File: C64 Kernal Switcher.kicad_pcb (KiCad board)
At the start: 2 copper layers, 20.3 x 47.6 mm, 12 parts, among them J1 Signals, J2 RGB, J3 LED, U1 2364, U2 PIC12F629, U3 27C256

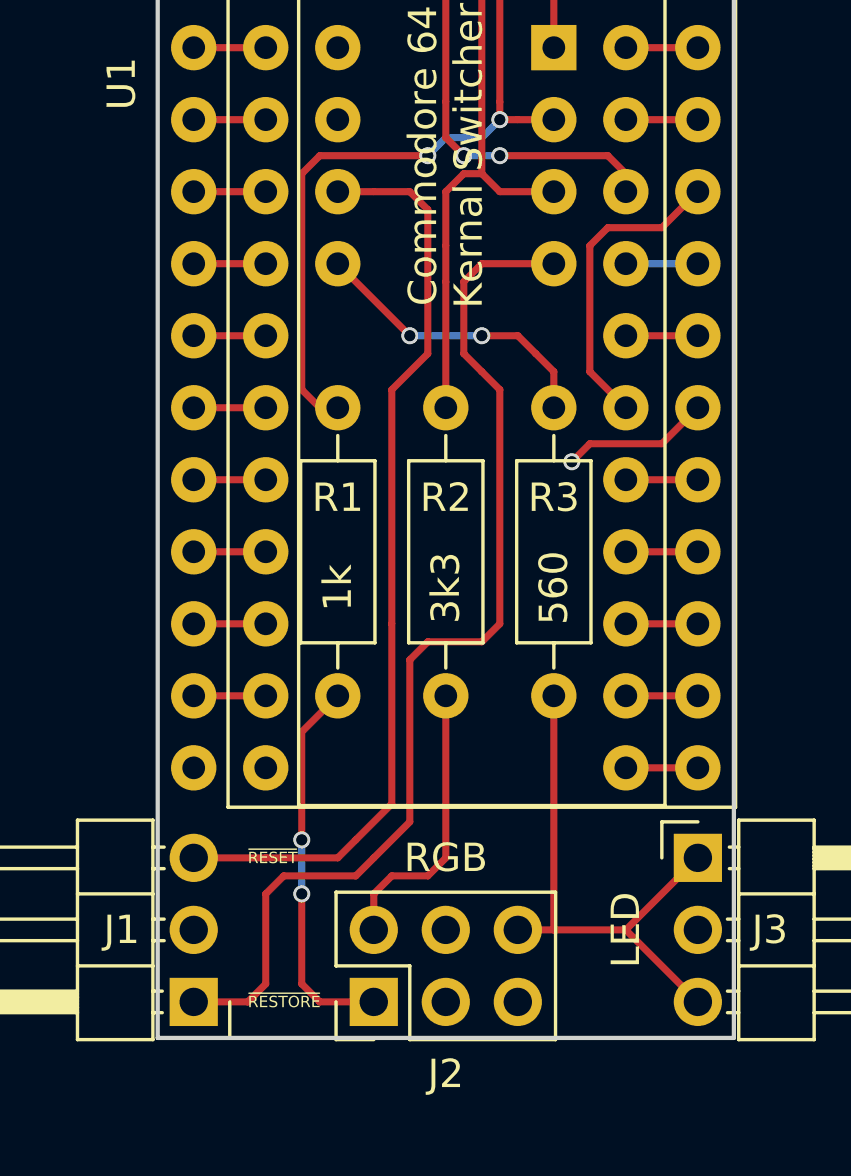
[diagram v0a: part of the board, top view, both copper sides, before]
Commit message: Moved R1 so it fits better under socket
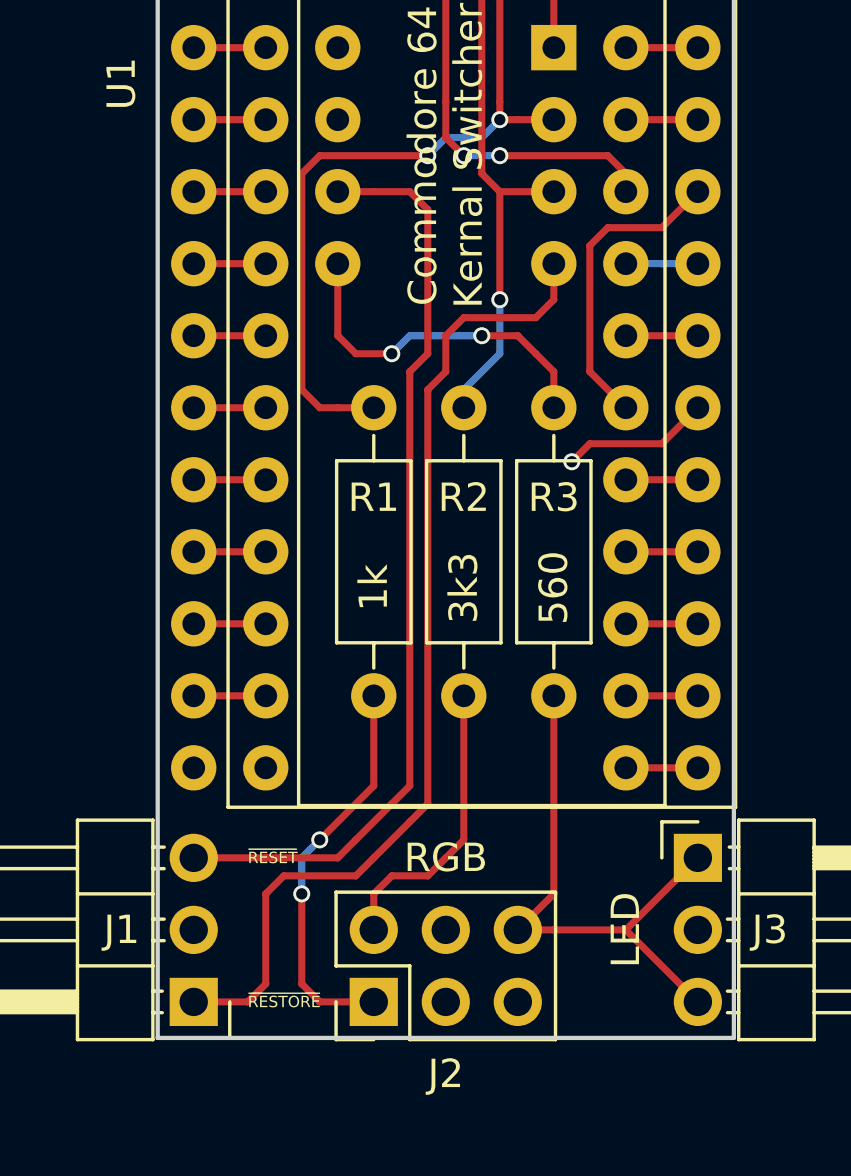
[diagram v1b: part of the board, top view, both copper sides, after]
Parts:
- moved R1 1.27 mm to (76.2, 99.1)
- moved R2 0.64 mm to (79.4, 99.1)
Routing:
- net ~RESTORE: track 37.6 -> 35.4 mm
- net Net-(R3-Pad2): track 10.5 -> 12.5 mm
- net A14: track 38.1 -> 39.4 mm
- net A13: track 41.5 -> 40.5 mm, vias 2 -> 3
- net RED: track 19.2 -> 19.8 mm
- net BLUE: track 13.5 -> 14.0 mm
